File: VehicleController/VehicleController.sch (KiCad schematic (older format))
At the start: 20 parts, among them P2 MX150_8, Q1 Q_PMOS_GDS, Q2 Q_NMOS_GDS, U1 Teensy_3.5, U16 H3LIS331DL, U5 BTS6133D, U6 UltimateSensorFusion

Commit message: Nearly finished with VC Schematic
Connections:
- net +3.3V is gone; now on net +3V3: U1.15 (3.3V), U1.46 (3.3V)
- net 3D_FIX: now also U1.11 (9(PWM/CS0/RX2)); no longer U1.4 (2(PWM))
- net GPS_RX: now also U1.10 (8(PWM/TX3)); no longer U1.3 (1(MISO1/TX1))
- net GPS_TX: now also U1.9 (7(PWM/RX3)); no longer U1.2 (0(MOSI1/RX1))
- net START_CAR: now also U1.2 (0(MOSI1/RX1)); no longer U1.8 (6(PWM))
- net CS0 renamed GPS_RST
- net MISO0: no longer names the net of U1.14 (12(MISO0))
- net MOSI0: no longer names the net of U1.13 (11(MOSI0))
- net SCK0: no longer names the net of U1.35 ((SCK0)/13)
- new net 1PPS: U1.8 (6(PWM))
- new net PRECHARGE: U1.3 (1(MISO1/TX1))
- no-connect marks 23 -> 26
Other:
- moved on the sheet: BT1, D2, F2, Q1, R4, R6, R7, R8

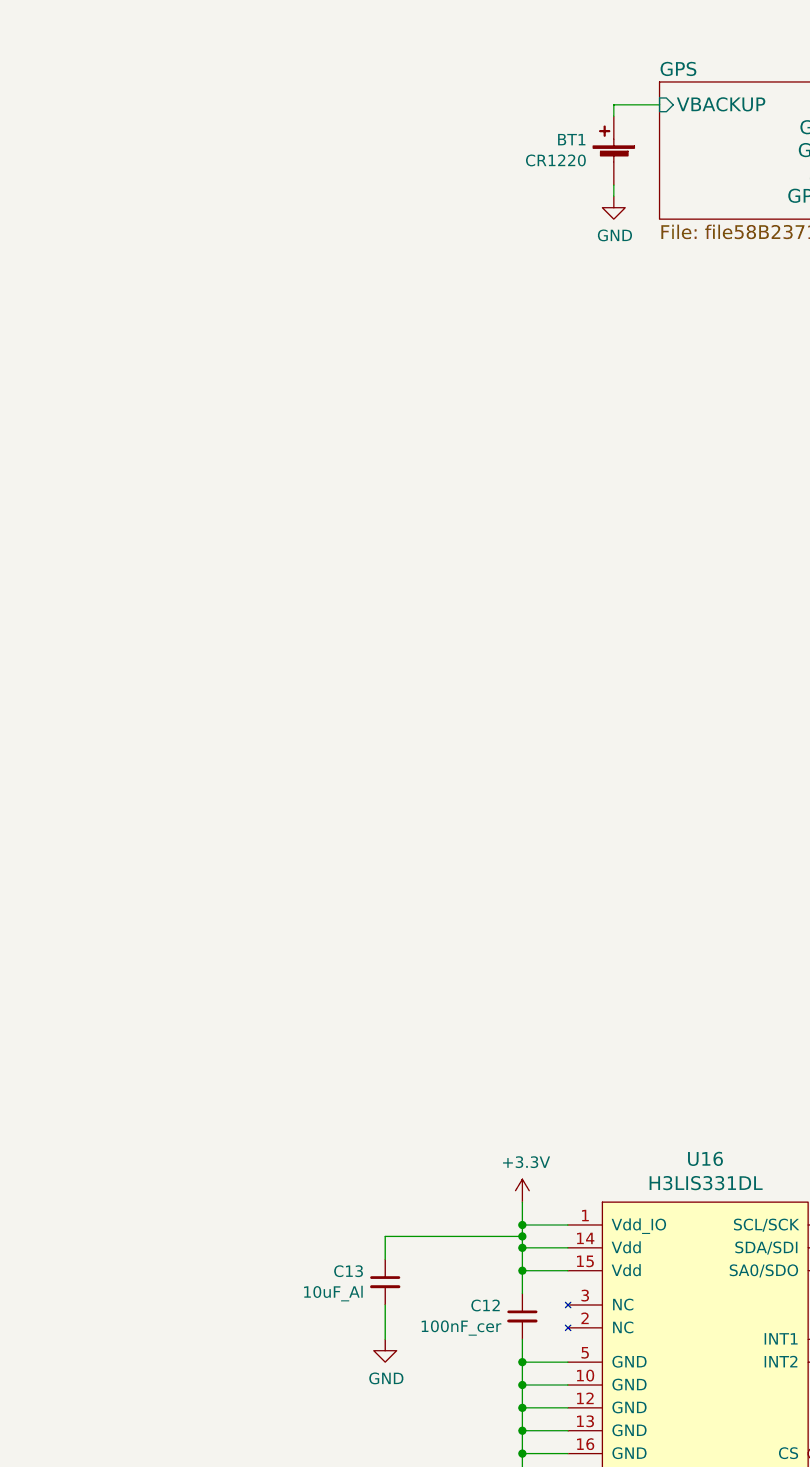
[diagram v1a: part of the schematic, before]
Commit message: More status LEDs and fuses
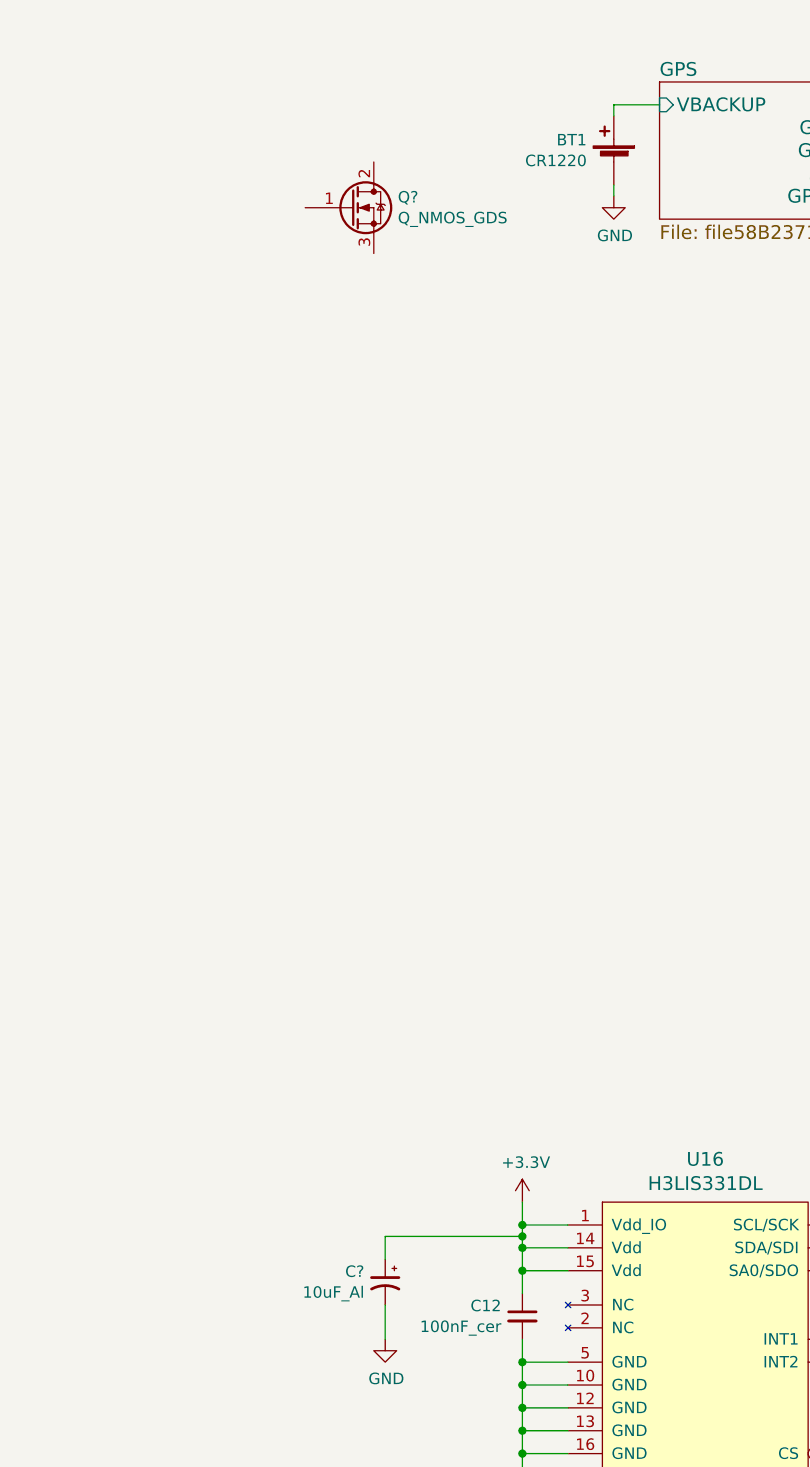
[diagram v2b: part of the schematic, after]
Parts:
- removed C13: 10uF_Al, symbol C_Small
- added C?: 10uF_Al, symbol CP1_Small
- added Q?: Q_NMOS_GDS, symbol Q_NMOS_GDS
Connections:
- net +3V3: now also C?.1
- net GND: now also C?.2
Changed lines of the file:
@@
 EESchema Schematic File Version 2
+LIBS:VehicleController-rescue
 LIBS:UNCAMotorsports
-LIBS:VehicleController-rescue
 LIBS:power
 LIBS:device
@@
 SHTDWN_IN
 $Comp
-L C_Small C13
-U 1 1 58BE72D2
-P 5600 8650
-F 0 "C13" H 5692 8696 50  0000 L CNN
-F 1 "10uF_Al" H 5692 8605 50  0000 L CNN
-F 2 "" H 5600 8650 50  0000 C CNN
-F 3 "" H 5600 8650 50  0000 C CNN
-	1    5600 8650
-	-1   0    0    -1
-$EndComp
-$Comp
 L GND #PWR020
 U 1 1 58BE950D
@@
 	900  2450 1250 2450
 Connection ~ 1250 2450
+$Comp
+L Q_NMOS_GDS Q?
+U 1 1 58C2CFE9
+P 5450 3950
+F 0 "Q?" H 5655 3996 50  0000 L CNN
+F 1 "Q_NMOS_GDS" H 5655 3905 50  0000 L CNN
+F 2 "" H 5650 4050 50  0000 C CNN
+F 3 "" H 5450 3950 50  0000 C CNN
+	1    5450 3950
+	1    0    0    -1
+$EndComp
+$Comp
+L CP1_Small C?
+U 1 1 58C40E3F
+P 5600 8650
+F 0 "C?" H 5691 8696 50  0000 L CNN
+F 1 "10uF_Al" H 5691 8605 50  0000 L CNN
+F 2 "" H 0   0   50  0001 C CNN
+F 3 "" H 0   0   50  0001 C CNN
+	1    5600 8650
+	-1   0    0    -1
+$EndComp
 $EndSCHEMATC

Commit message: Begin nailing down VC schematic details
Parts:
- removed Q?: Q_NMOS_GDS, symbol Q_NMOS_GDS
- added D2: SCL0, symbol LED_Small_ALT
- added D3: SDA0, symbol LED_Small_ALT
- added R2: 0R, symbol R_Small
- added R8, R9: 220, symbol R_Small
- added U5: NDC7003P, symbol NDC7003P
- C2: renamed from C12; value 100nF_cer -> 100nF
- gave numbers to parts that had none: 1
- renumbered C5 to C3, C2 to C4, D2 to D1, F2 to F1, P2 to P1, Q2 to Q1, Q1 to Q2, R6 to R1, R5 to R3, R19 to R4, R4 to R5, R7 to R6, R8 to R7, U5 to U1, U16 to U2, U6 to U3, U1 to U4
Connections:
- net +3V3: now also U5.2 (S2), U5.5 (S1)
- net GND: now also D2.1 (K), D3.1 (K)
- net SCL0: now also U5.1 (G1)
- net SDA0: now also U5.3 (G2)
- net at U1.2 (IN): now also R2.1; no longer Q1.2 (D)
- new net: Q1.2 (D), R2.2
- new net: R9.2, U5.4 (D2)
- new net: R8.2, U5.6 (D1)
- new net: D2.2 (A), R8.1
- new net: D3.2 (A), R9.1
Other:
- note added: "I2C Pull-up Resistors \nincluded on Sensor Fusion\nBreakout"
- moved on the sheet: C1, Q1, R1

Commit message: Finish VCU schematic, most footprint selections.  Start layout
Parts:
- C1: footprint (none) -> Capacitors_SMD:c_elec_5x5.8
- C2: footprint (none) -> Capacitors_SMD:C_0805_HandSoldering
- C3, C4: value C_Small -> 1uF; footprint (none) -> Capacitors_SMD:C_0805_HandSoldering
- D1: footprint (none) -> Diodes_SMD:SMA_Handsoldering
- D2, D3: footprint (none) -> LEDs:LED-0805
- F1: footprint (none) -> Fuse_Holders_and_Fuses:Fuse_SMD1206_HandSoldering
- P1: footprint (none) -> UNCAMotorsports:MX150_8Pin
- Q1: value Q_NMOS_GDS -> Shutdown_FET; footprint (none) -> TO_SOT_Packages_SMD:SOT-23_Handsoldering
- Q2: footprint (none) -> TO_SOT_Packages_SMD:SOT-23_Handsoldering
- R1, R5: value R_Small -> 10k; footprint (none) -> Resistors_SMD:R_0805_HandSoldering
- R2, R3, R4, R6, R7, R8, R9: footprint (none) -> Resistors_SMD:R_0805_HandSoldering
- U1: footprint (none) -> UNCAMotorsports:TO-252-5
- U2: footprint (none) -> UNCAMotorsports:LGA-16-3x3
- U4: footprint (none) -> UNCAMotorsports:Teensy_3.5
- U5: footprint (none) -> TO_SOT_Packages_SMD:SOT-23-6

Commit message: ESF Fixes
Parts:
- added Q6: AIR_FET, TO_SOT_Packages_SMD:SOT-23_Handsoldering, symbol Q_NMOS_GDS
- added R30: 10k, Resistors_SMD:R_0805_HandSoldering, symbol R_Small
- added R31: 0R, Resistors_SMD:R_0805_HandSoldering, symbol R_Small
- added R32: 1k, Resistors_SMD:R_0805_HandSoldering, symbol R_Small
- added U21: BTS6133D, symbol BTS6133D
- U3: footprint (none) -> UNCAMotorsports:UltimateSensorFusion
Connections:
- net GND: now also Q6.3 (S), R30.2, R32.2
- net PRECHARGE: no longer U4.3 (1(MISO1/TX1))
- net TSMS: now reaches P1.6 (P4)
- net TSMS: now also U21.3 (VBB)
- net AIR+: now reaches P1.7 (P6)
- net AIR+: now also U21.1 (OUT), U21.5 (OUT)
- new net: R31.1, U21.2 (IN)
- new net: R32.1, U21.4 (IS)
- new net: Q6.2 (D), R31.2
- new net CLOSE_AIR: Q6.1 (G), R30.1, U4.3 (1(MISO1/TX1))
- no-connect marks 26 -> 24

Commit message: VCU Changes post ESF
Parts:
- removed Q2: Q_PMOS_GDS, TO_SOT_Packages_SMD:SOT-23_Handsoldering, symbol Q_PMOS_GDS
- added Q2: Buzzer_FET, TO_SOT_Packages_SMD:SOT-23_Handsoldering, symbol Q_NMOS_GDS
- R5: footprint Resistors_SMD:R_0805_HandSoldering -> (none)
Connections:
- net BUZZER_OUT: now also F1.2
- net DAC_LATCH: now also U4.31 (A20/39); no longer U4.28 ((PWM)A17/36)
- net GND: now also R5.2, Q2.3 (S)
- net at U4.24 (32/A13(SCK1/TX4)): now also D1.1 (K), R6.1, R7.2
- net Isolation/F_R1: now reaches U4.26 ((RX5)A15/34)
- net Isolation/F_L2: now reaches U4.27 ((PWM)A16/35)
- net PC_CTRL: now reaches U4.4 (2(PWM))
- net BUZZ_CTRL: now reaches R5.1
- net BUZZ_CTRL: now also U4.7 (5(PWM)), Q2.1 (G); no longer F1.2
- removed net BUZZER: R5.2, U4.7 (5(PWM))
- new net BUZZER_IN: Q2.2 (D)
- new net Isolation/F_L1: U4.28 ((PWM)A17/36)
- new net Isolation/F_R2: U4.25 ((TX5)A14/33)
- no-connect marks 24 -> 19
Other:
- moved on the sheet: C3, D1, F1, R6, R7

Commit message: TestMule schematic for skillshare
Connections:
- net IMD_FAULT: now reaches U4.16 (24)
- net AMS_FAULT: now reaches U4.17 (25)
- no-connect marks 19 -> 15
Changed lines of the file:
@@
 	-1   0    0    -1
 $EndComp
-NoConn ~ 9550 4300
-NoConn ~ 9550 4400
-NoConn ~ 9550 4500
-NoConn ~ 9550 4600
 NoConn ~ 9550 4700
 NoConn ~ 9550 4800
@@
 Connection ~ 11900 2800
 Wire Wire Line
-	11750 2800 11900 2800
-Wire Wire Line
-	11900 2800 12050 2800
+	11750 2800 12050 2800
 Wire Wire Line
 	11900 2600 11900 2800
@@
 	7800 3800 9550 3800
 Wire Wire Line
-	9900 8300 9900 8400
-Wire Wire Line
-	9900 8400 9900 8500
+	9900 8300 9900 8500
 Wire Wire Line
 	9900 8400 9300 8400
 Wire Wire Line
-	9900 8700 9900 8800
-Wire Wire Line
-	9900 8800 9900 8900
+	9900 8700 9900 8900
 Wire Wire Line
 	9900 8800 9300 8800
@@
 	8950 3400 9550 3400
 Wire Wire Line
-	3550 2950 3650 2950
-Wire Wire Line
-	3650 2950 4250 2950
+	3550 2950 4250 2950
 Wire Wire Line
 	3550 3050 3650 3050
@@
 	1400 4000 1400 3900
 Wire Wire Line
-	800  3900 1400 3900
-Wire Wire Line
-	1400 3900 1450 3900
-Wire Wire Line
-	1750 4100 1750 4250
-Wire Wire Line
-	1750 4250 1750 4350
+	800  3900 1450 3900
+Wire Wire Line
+	1750 4100 1750 4350
 Wire Wire Line
 	1400 4200 1400 4250
@@
 	2650 3250 2650 3150
 Wire Wire Line
-	1900 3150 2650 3150
-Wire Wire Line
-	2650 3150 2750 3150
+	1900 3150 2750 3150
 Wire Wire Line
 	2650 3550 2650 3450
@@
 	8350 5350 8450 5350
 Wire Wire Line
-	8750 5350 8800 5350
-Wire Wire Line
-	8800 5350 8900 5350
-Wire Wire Line
-	8900 5350 9000 5350
+	8750 5350 9000 5350
 Wire Wire Line
 	8800 5350 8800 5100
@@
 Connection ~ 8900 5350
 Wire Wire Line
-	9400 5350 9400 5500
-Wire Wire Line
-	9400 5500 9400 5600
+	9400 5350 9400 5600
 Wire Wire Line
 	9400 5350 9300 5350
@@
 	6400 9000 6200 9000
 Wire Wire Line
-	6200 8900 6200 9000
-Wire Wire Line
-	6200 9000 6200 9100
-Wire Wire Line
-	6200 9100 6200 9200
-Wire Wire Line
-	6200 9200 6200 9300
-Wire Wire Line
-	6200 9300 6200 9400
-Wire Wire Line
-	6200 9400 6200 9600
+	6200 8900 6200 9600
 Wire Wire Line
 	6400 9400 6200 9400
@@
 Connection ~ 6200 9100
 Wire Wire Line
-	6200 8200 6200 8300
-Wire Wire Line
-	6200 8300 6200 8400
-Wire Wire Line
-	6200 8400 6200 8500
-Wire Wire Line
-	6200 8500 6200 8600
-Wire Wire Line
-	6200 8600 6200 8700
+	6200 8200 6200 8700
 Wire Wire Line
 	6200 8400 6400 8400
@@
 	1250 1750 1250 1950
 Wire Wire Line
-	900  1950 1250 1950
-Wire Wire Line
-	1250 1950 1350 1950
-Wire Wire Line
-	1250 2250 1250 2450
-Wire Wire Line
-	1250 2450 1250 2500
+	900  1950 1350 1950
+Wire Wire Line
+	1250 2250 1250 2500
 Wire Wire Line
 	1250 2250 1350 2250
@@
 	1850 2250 2450 2250
 Wire Wire Line
-	7200 2300 7300 2300
-Wire Wire Line
-	7300 2300 7850 2300
+	7200 2300 7850 2300
 Wire Wire Line
 	1850 1950 2450 1950
@@
 	14250 3350 14350 3350
 Wire Wire Line
-	14750 3350 14750 3550
-Wire Wire Line
-	14750 3550 14750 3650
+	14750 3350 14750 3650
 Wire Wire Line
 	14750 3350 14550 3350
@@
 Connection ~ 14750 3550
 Wire Wire Line
-	13100 3200 13100 3300
-Wire Wire Line
-	13100 3300 13100 3400
+	13100 3200 13100 3400
 Wire Wire Line
 	13100 3300 13250 3300
@@
 $EndComp
 Wire Wire Line
-	3550 4850 3650 4850
-Wire Wire Line
-	3650 4850 3950 4850
+	3550 4850 3950 4850
 Wire Wire Line
 	3550 4950 3650 4950
@@
 	1900 5600 1900 5500
 Wire Wire Line
-	1400 5500 1900 5500
-Wire Wire Line
-	1900 5500 1950 5500
-Wire Wire Line
-	2250 5700 2250 5850
-Wire Wire Line
-	2250 5850 2250 5950
+	1400 5500 1950 5500
+Wire Wire Line
+	2250 5700 2250 5950
 Wire Wire Line
 	1900 5800 1900 5850
@@
 Text Label 1400 5500 0    60   ~ 0
 CLOSE_AIR
-$Comp
-L Teensy_3.5 U4
-U 1 1 587C74D8
-P 10650 3950
-F 0 "U4" H 10650 5387 60  0000 C CNN
-F 1 "Teensy_3.5" H 10650 5281 60  0000 C CNN
-F 2 "UNCAMotorsports:Teensy_3.5" H 11100 4650 60  0001 C CNN
-F 3 "" H 11100 4650 60  0000 C CNN
-	1    10650 3950
-	1    0    0    -1
-$EndComp
 Wire Wire Line
 	11750 4800 12450 4800
@@
 	7300 2650 6900 2650
 Wire Wire Line
-	6900 2500 6900 2650
-Wire Wire Line
-	6900 2650 6900 2750
+	6900 2500 6900 2750
 $Comp
 L GND #PWR15
@@
 Text Label 8950 3100 0    60   ~ 0
 PC_CTRL
+$Comp
+L Teensy_3.5 U4
+U 1 1 587C74D8
+P 10650 3950
+F 0 "U4" H 10650 5387 60  0000 C CNN
+F 1 "Teensy_3.5" H 10650 5281 60  0000 C CNN
+F 2 "UNCAMotorsports:Teensy_3.5" H 11100 4650 60  0001 C CNN
+F 3 "" H 11100 4650 60  0000 C CNN
+	1    10650 3950
+	1    0    0    -1
+$EndComp
+Wire Wire Line
+	9550 4300 8950 4300
+Text Label 8950 4300 0    60   ~ 0
+IMD_FAULT
+Wire Wire Line
+	9550 4400 8950 4400
+Text Label 8950 4400 0    60   ~ 0
+AMS_FAULT
 $EndSCHEMATC

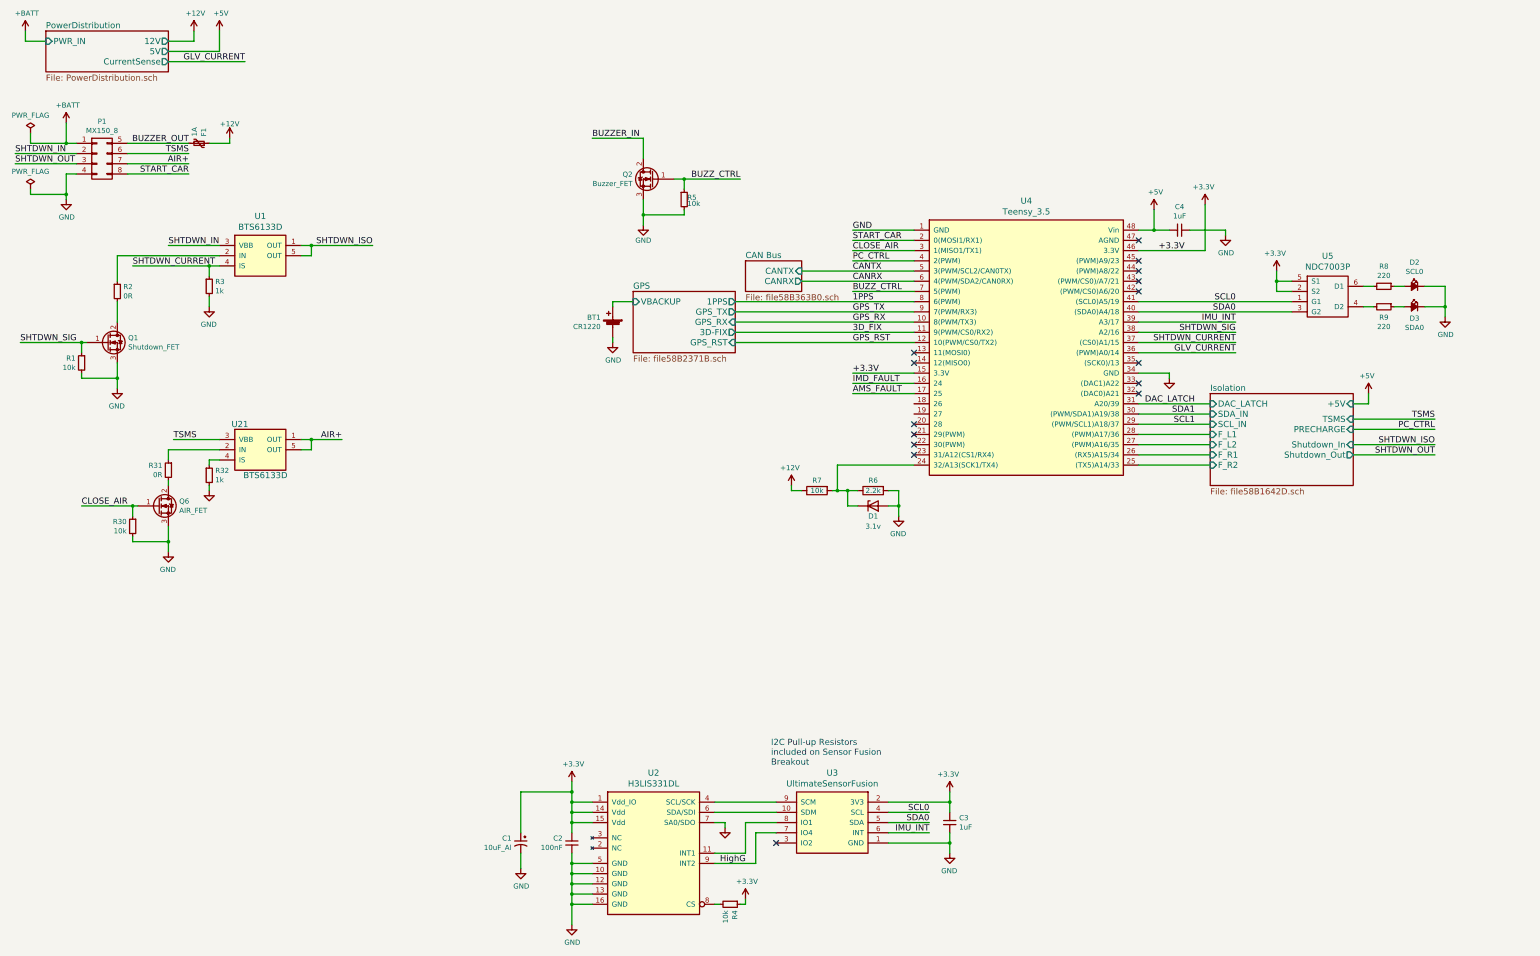
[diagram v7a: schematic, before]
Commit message: Add reset switch on VCU
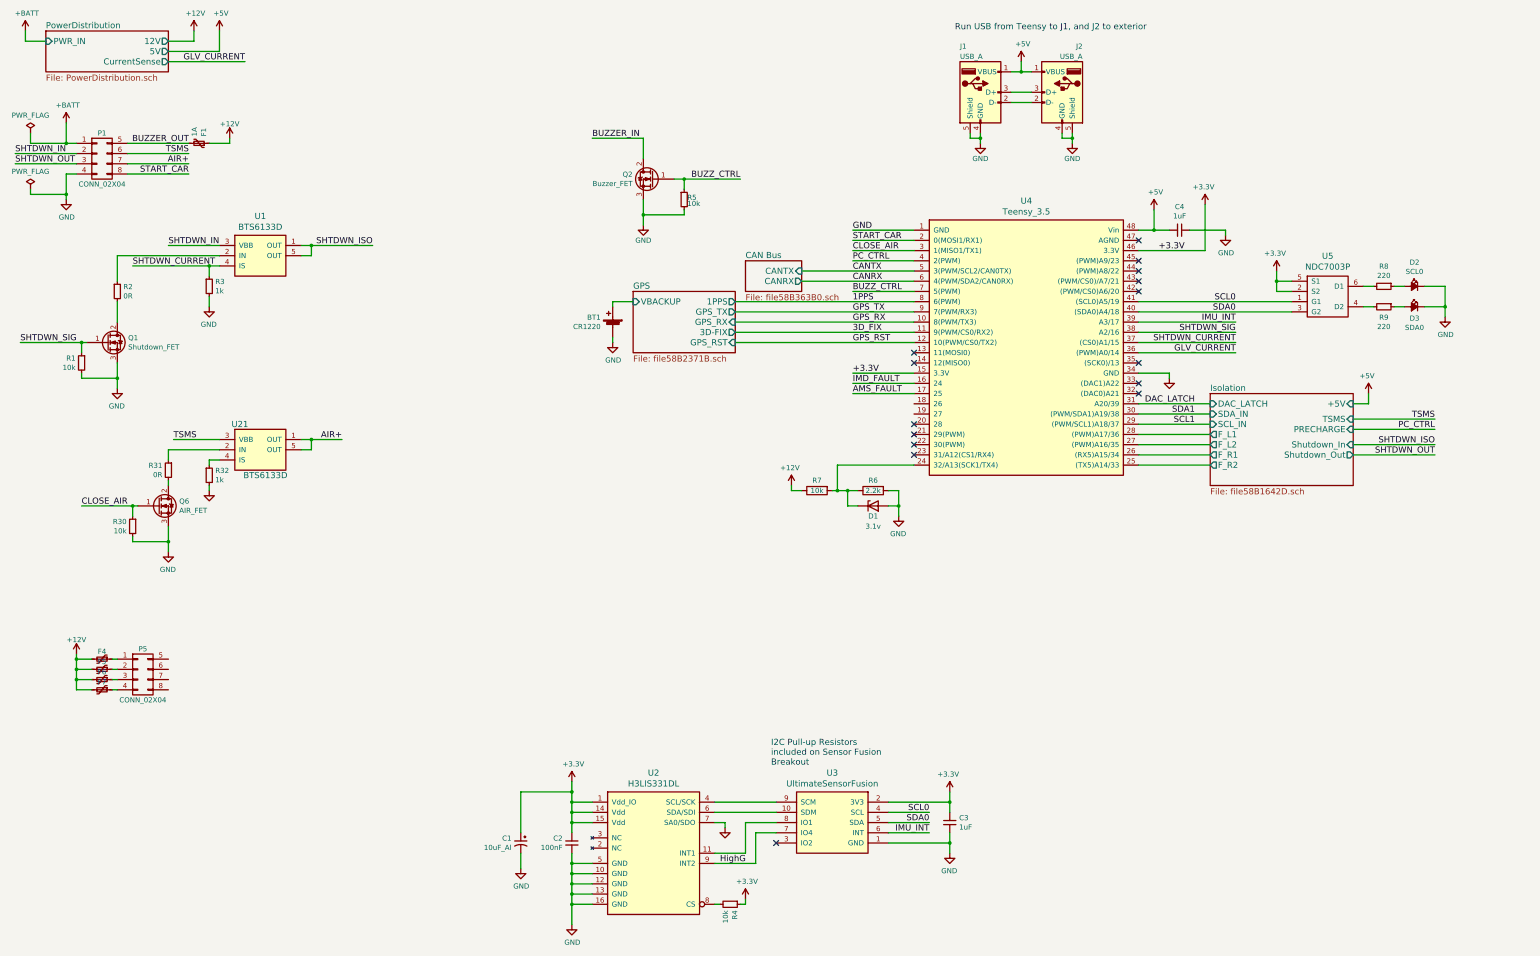
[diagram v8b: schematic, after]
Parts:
- removed P1: MX150_8, UNCAMotorsports:MX150_8Pin, symbol MX150_8
- added F4: 1A, symbol Polyfuse_Small
- added F5, F6, F7: Polyfuse_Small, symbol Polyfuse_Small
- added J1, J2: USB_A, symbol USB_A
- added P1, P5: CONN_02X04, symbol CONN_02X04
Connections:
- net +12V: now also F4.2, F5.2, F6.2, F7.2
- net +5V: now also J1.1 (VBUS), J2.1 (VBUS)
- net +BATT: now also P1.1 (P1)
- net AIR+: now also P1.7 (P6)
- net BUZZER_OUT: now also P1.5 (P2)
- net GND: now also J1.4 (GND), J1.5 (Shield), J2.4 (GND), J2.5 (Shield), P1.4 (P7)
- net SHTDWN_IN: now also P1.2 (P3)
- net SHTDWN_OUT: now also P1.3 (P5)
- net START_CAR: now also P1.8 (P8)
- net TSMS: now also P1.6 (P4)
- new net: F4.1, P5.1 (P1)
- new net: F5.1, P5.2 (P3)
- new net: F6.1, P5.3 (P5)
- new net: F7.1, P5.4 (P7)
- new net: J1.2 (D-), J2.2 (D-)
- new net: J1.3 (D+), J2.3 (D+)
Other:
- note added: "Run USB from Teensy to J1, and J2 to exterior"
